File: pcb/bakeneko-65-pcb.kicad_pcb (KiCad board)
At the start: 2 copper layers, 303.8 x 94.2 mm, 161 parts, among them J1 JST SH 4-pin, J2 AVR-ISP-6, SW1 Reset, U1 SRV05-4, U2 ATmega32U4-AU, Y1 16MHz

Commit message: switched to alps footprints
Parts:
- removed MX33: 1.25u, MX_Only:MXOnly-1.25U-NoLED
- MX1, MX10, MX11, MX12, MX13, MX14, MX15, MX16, MX19, MX2, MX20, MX21, MX22, MX23, MX24, MX25, MX26, MX27, MX28, MX29, MX3, MX30, MX32, MX35, MX36, MX37, MX38, MX39, MX4, MX40, MX41, MX42, MX43, MX44, MX45, MX47, MX49, MX5, MX50, MX51, MX52, MX53, MX54, MX55, MX56, MX57, MX58, MX6, MX60, MX61, MX63, MX68, MX69, MX7, MX70, MX8, MX9: footprint MX_Only:MXOnly-1U-NoLED -> Alps_Only:ALPS-1U
- MX17: footprint MX_Only:MXOnly-2U-NoLED -> Alps_Only:ALPS-2U
- MX18, MX31, MX62, MX64, MX67: footprint MX_Only:MXOnly-1.5U-NoLED -> Alps_Only:ALPS-1.5U
- MX34, MX59: footprint MX_Only:MXOnly-1.75U-NoLED -> Alps_Only:ALPS-1.75U
- MX46, MX48: footprint MX_Only:MXOnly-2.25U-NoLED -> Alps_Only:ALPS-2.25U
- MX65: footprint MX_Only:MXOnly-7U-ReversedStabilizers-NoLED -> Alps_Only:ALPS-7U
- MX66, MX71, MX72, MX73, MX75: footprint MX_Only:MXOnly-1.25U-NoLED -> Alps_Only:ALPS-1.25U
- MX74: footprint MX_Only:MXOnly-6.25U-ReversedStabilizers-NoLED -> Alps_Only:ALPS-6.25U
- moved D66 83.8 mm to (341.2, 120.0)
- moved MX14 83.8 mm to (333.3, 43.0)
- moved MX68 83.8 mm to (333.3, 119.2)
- moved D11 83.8 mm to (266.6, 43.8)
- moved D12 83.8 mm to (285.6, 43.8)
- moved D35 83.8 mm to (147.5, 81.9)
- moved D40 83.8 mm to (242.8, 81.9)
- moved D41 83.8 mm to (261.8, 81.9)
- moved D51 83.8 mm to (195.1, 100.9)
- moved D53 83.8 mm to (233.2, 100.9)
- moved D56 83.8 mm to (290.4, 100.9)
- moved D6 83.8 mm to (171.3, 43.8)
- moved D8 83.8 mm to (209.4, 43.8)
- moved MX22 83.8 mm to (171.3, 62.0)
- moved MX24 83.8 mm to (209.4, 62.0)
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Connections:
- U1 pad 3: Net-(U1-Pad3) -> unconnected-(U1-IO2-Pad3)
- U1 pad 4: Net-(U1-Pad4) -> unconnected-(U1-IO3-Pad4)
- U2 pad 41: Net-(U2-Pad41) -> unconnected-(U2-PF0-Pad41)
- U2 pad 42: Net-(U2-Pad42) -> unconnected-(U2-AREF-Pad42)
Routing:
- net Net-(D32-A): track 19.7 -> 11.7 mm
- net Net-(D63-A): track 18.7 -> 21.5 mm
- net Net-(D57-A): track 6.82 -> 8.33 mm
- net Net-(D42-A): track 6.82 -> 8.33 mm
- net Net-(D13-A): track 6.82 -> 8.33 mm
- net Net-(D26-A): track 6.82 -> 8.33 mm
- net Net-(D43-A): track 6.82 -> 8.33 mm
- net Net-(D39-A): track 6.82 -> 8.33 mm
- net Net-(D14-A): track 6.82 -> 8.33 mm
- net Net-(D10-A): track 6.82 -> 8.33 mm
- net Net-(D27-A): track 6.82 -> 8.33 mm
- net Net-(D36-A): track 6.82 -> 8.33 mm
- net Net-(D58-A): track 6.82 -> 8.33 mm
- net Net-(D55-A): track 6.82 -> 8.33 mm
- net Net-(D7-A): track 6.82 -> 8.33 mm
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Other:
- net class D removed
- net class Default removed
- net class Power removed

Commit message: fixing library issues
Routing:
- net Net-(D54-A): track 6.82 -> 8.33 mm
- net +5V: track 123.2 -> 122.5 mm

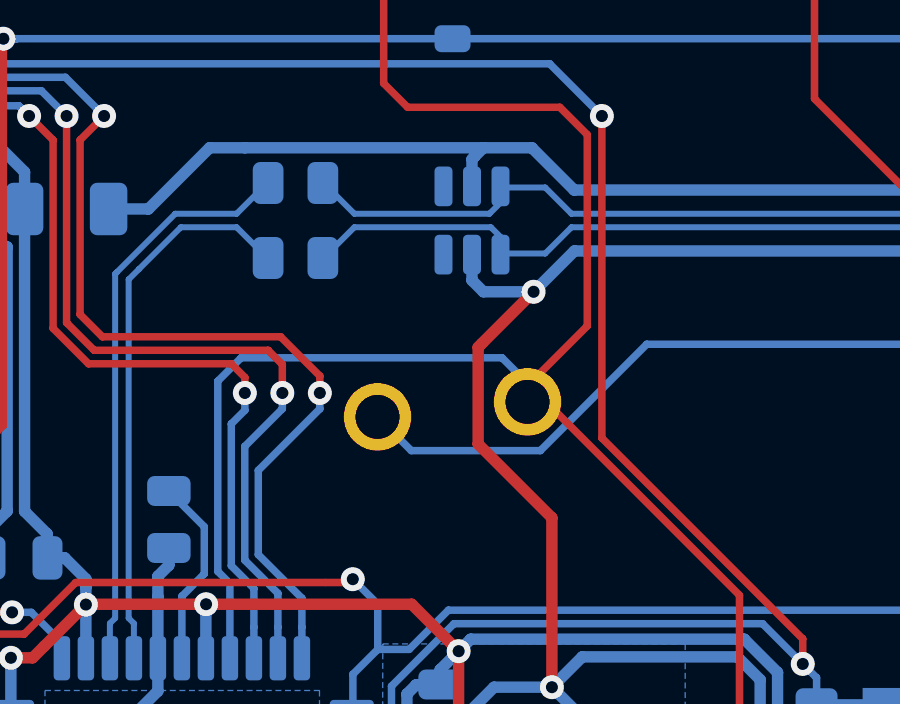
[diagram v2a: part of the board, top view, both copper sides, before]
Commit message: fix clearance issues from updated footprints
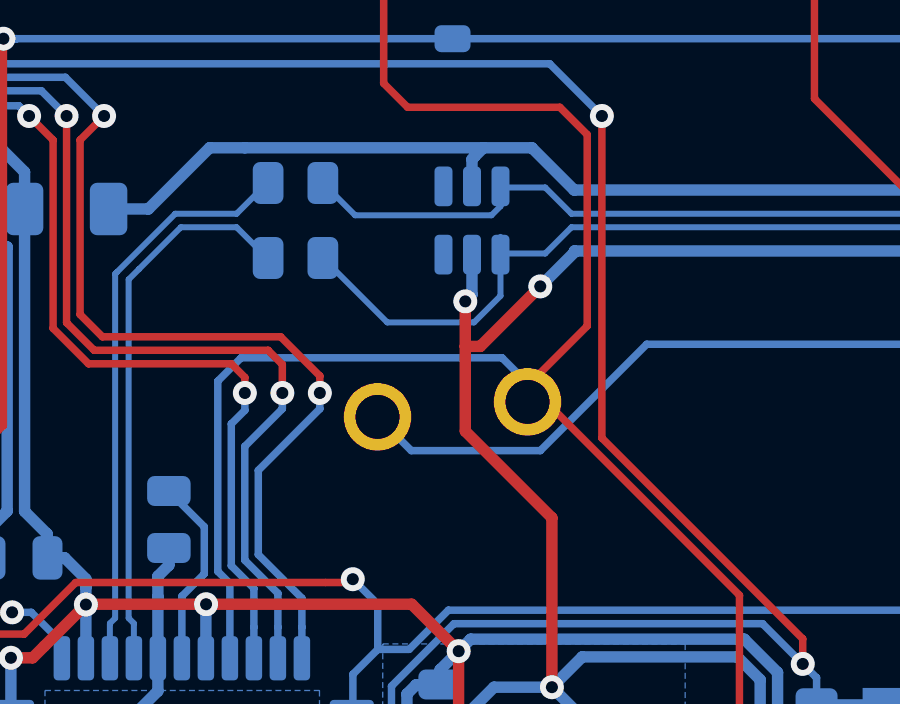
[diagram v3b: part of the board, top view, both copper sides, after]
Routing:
- net D+: track 32.4 -> 34.5 mm
- net GND: track 184.5 -> 185.2 mm, vias 5 -> 6
- net D-: track 32.3 -> 33.0 mm
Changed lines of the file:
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@@
 		)
 		(fp_text user "${REFERENCE}"
-			(at 0 0 180)
+			(at 0 0 0)
 			(layer "B.Fab")
 			(effects
@@
 	)
 	(segment
-		(start 115.0325 55.70875)
-		(end 115.159608 55.581642)
+		(start 108.0175 88.61)
+		(end 108.0175 84.14)
 		(width 0.381)
 		(layer "F.Cu")
@@
 	)
 	(segment
-		(start 108.0175 88.61)
-		(end 108.0175 84.14)
+		(start 114.60375 55.68)
+		(end 114.60375 54.18)
 		(width 0.381)
 		(layer "F.Cu")
@@
 	)
 	(segment
-		(start 115.0325 58.935)
-		(end 115.0325 55.70875)
+		(start 117.10375 53.68)
+		(end 115.10375 55.68)
 		(width 0.381)
 		(layer "F.Cu")
@@
 	(segment
 		(start 117.49125 61.39375)
-		(end 115.0325 58.935)
+		(end 114.60375 58.50625)
 		(width 0.381)
 		(layer "F.Cu")
@@
 	)
 	(segment
-		(start 115.159608 55.581642)
-		(end 116.88125 53.86)
+		(start 117.49125 67.04)
+		(end 117.49125 61.39375)
 		(width 0.381)
 		(layer "F.Cu")
@@
 	)
 	(segment
-		(start 117.49125 67.04)
-		(end 117.49125 61.39375)
+		(start 114.60375 58.50625)
+		(end 114.60375 55.68)
+		(width 0.381)
+		(layer "F.Cu")
+		(net 1)
+	)
+	(segment
+		(start 115.10375 55.68)
+		(end 114.60375 55.68)
 		(width 0.381)
 		(layer "F.Cu")
@@
 	)
 	(via
-		(at 117.49125 67.04)
+		(at 117.10375 53.68)
 		(size 0.8)
 		(drill 0.4)
@@
 	)
 	(via
-		(at 116.88125 53.86)
+		(at 117.49125 67.04)
 		(size 0.8)
 		(drill 0.4)
@@
 		(net 1)
 	)
+	(via
+		(at 114.60375 54.18)
+		(size 0.8)
+		(drill 0.4)
+		(layers "F.Cu" "B.Cu")
+		(net 1)
+	)
 	(segment
 		(start 116.46375 72.5)
@@
 	)
 	(segment
-		(start 116.88125 53.86)
-		(end 118.24199 52.49926)
-		(width 0.381)
-		(layer "B.Cu")
-		(net 1)
-	)
-	(segment
 		(start 128.6975 71.365)
 		(end 126.35875 71.365)
@@
 	)
 	(segment
-		(start 115.2075 53.86)
-		(end 116.88125 53.86)
+		(start 118.24199 52.49926)
+		(end 118.24199 52.54176)
 		(width 0.381)
 		(layer "B.Cu")
@@
 	)
 	(segment
+		(start 118.24199 52.54176)
+		(end 117.10375 53.68)
+		(width 0.381)
+		(layer "B.Cu")
+		(net 1)
+	)
+	(segment
 		(start 118.66375 70.8)
 		(end 118.66375 69.0125)
@@
 	)
 	(segment
+		(start 114.8275 52.62125)
+		(end 114.8275 53.95625)
+		(width 0.381)
+		(layer "B.Cu")
+		(net 1)
+	)
+	(segment
 		(start 119.74475 70.8)
 		(end 120.23375 71.289)
@@
 	)
 	(segment
+		(start 114.8275 53.95625)
+		(end 114.60375 54.18)
+		(width 0.381)
+		(layer "B.Cu")
+		(net 1)
+	)
+	(segment
 		(start 104.3575 63.34125)
 		(end 104.3575 64.02625)
@@
 	)
 	(segment
-		(start 114.8275 53.48)
-		(end 115.2075 53.86)
-		(width 0.381)
-		(layer "B.Cu")
-		(net 1)
-	)
-	(segment
 		(start 98.89824 51.99031)
 		(end 99.27344 52.36551)
@@
 	)
 	(segment
-		(start 114.8275 52.58375)
-		(end 114.8275 53.48)
-		(width 0.381)
-		(layer "B.Cu")
-		(net 1)
-	)
-	(segment
 		(start 118.466652 70.8)
 		(end 118.66375 70.8)
@@
 	)
 	(segment
-		(start 115.45625 51.70875)
-		(end 115.7775 52.03)
-		(width 0.2)
-		(layer "B.Cu")
-		(net 77)
-	)
-	(segment
 		(start 115.7775 52.03)
 		(end 115.7775 52.58375)
@@
 	)
 	(segment
-		(start 110.90625 51.70875)
-		(end 115.45625 51.70875)
+		(start 109.85625 52.73375)
+		(end 112.0035 54.881)
 		(width 0.2)
 		(layer "B.Cu")
@@
 	)
 	(segment
-		(start 109.88125 52.73375)
-		(end 110.90625 51.70875)
+		(start 114.894114 54.881)
+		(end 115.7775 53.997614)
 		(width 0.2)
 		(layer "B.Cu")
@@
 	)
 	(segment
+		(start 112.0035 54.881)
+		(end 114.894114 54.881)
+		(width 0.2)
+		(layer "B.Cu")
+		(net 77)
+	)
+	(segment
 		(start 117.268751 52.58375)
 		(end 115.7775 52.58375)
@@
 	)
 	(segment
+		(start 115.7775 53.997614)
+		(end 115.7775 52.62125)
+		(width 0.2)
+		(layer "B.Cu")
+		(net 77)
+	)
+	(segment
 		(start 139.77875 50.98375)
 		(end 139.50375 51.25875)
@@
 	)
 	(segment
-		(start 115.40875 51.25875)
-		(end 115.7775 50.89)
+		(start 109.85625 50.23375)
+		(end 110.93225 51.30975)
 		(width 0.2)
 		(layer "B.Cu")
@@
 	)
 	(segment
-		(start 109.88125 50.23375)
-		(end 110.90625 51.25875)
+		(start 115.476499 51.30975)
+		(end 115.7775 51.008749)
 		(width 0.2)
 		(layer "B.Cu")
@@
 	)
 	(segment
+		(start 115.7775 51.008749)
+		(end 115.7775 50.34625)
+		(width 0.2)
+		(layer "B.Cu")
+		(net 78)
+	)
+	(segment
 		(start 118.143751 51.25875)
 		(end 117.268751 50.38375)
@@
 	)
 	(segment
-		(start 110.90625 51.25875)
-		(end 115.40875 51.25875)
+		(start 110.93225 51.30975)
+		(end 115.476499 51.30975)
 		(width 0.2)
 		(layer "B.Cu")
